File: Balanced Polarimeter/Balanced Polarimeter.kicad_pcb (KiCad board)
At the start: 2 copper layers, 65 x 46.5 mm, 23 parts, among them IC1 OP27, J1 73100-0105, J2 Conn_01x03_Pin, J3 Conn_01x02_Pin, J5 Conn_01x02_Pin, Q1 MMPQ3904, Q2 MMPQ3904, U1 ADA4898-1YRDZ, U2 ADA4898-1YRDZ

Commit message: Revised Wiring
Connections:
- D1 pad 1: Net-(D1-K) -> -5V
- D1 pad 3: +5V -> Net-(D1-A)
- D2 pad 1: Net-(D2-K) -> -5V
- D2 pad 3: +5V -> Net-(D2-A)
- Q1 pad 1: Net-(Q1-BASE_#2) -> Net-(D2-A)
- Q1 pad 13: Net-(Q1-BASE_#2) -> Net-(D2-A)
- Q1 pad 2: Net-(Q1-BASE_#2) -> Net-(D2-A)
- Q1 pad 3: Net-(D2-K) -> +5V
- Q1 pad 4: Net-(D2-K) -> +5V
- Q2 pad 1: Net-(Q2-BASE_#2) -> Net-(D1-A)
- Q2 pad 13: Net-(Q2-BASE_#2) -> Net-(D1-A)
- Q2 pad 2: Net-(Q2-BASE_#2) -> Net-(D1-A)
- Q2 pad 3: Net-(D1-K) -> +5V
- Q2 pad 4: Net-(D1-K) -> +5V
- R3 pad 2: Net-(U1--) -> Net-(Q1-COLLECTOR_#3_1)
- R4 pad 2: Net-(U2--) -> Net-(Q2-COLLECTOR_#3_1)
- U1 pad 2: Net-(U1--) -> Net-(Q1-COLLECTOR_#3_1)
- U1 pad 3: Net-(Q1-COLLECTOR_#3_1) -> GND
- U2 pad 2: Net-(U2--) -> Net-(Q2-COLLECTOR_#3_1)
- U2 pad 3: Net-(Q2-COLLECTOR_#3_1) -> GND
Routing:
- net -5V: track 105.2 -> 176.9 mm, vias 0 -> 1
- net Net-(Q1-COLLECTOR_#3_1): track 28.3 -> 59.9 mm, vias 2 -> 1
- net Net-(D1-A): track 0.00 -> 29.1 mm
- net Net-(D2-A): track 0.00 -> 27.1 mm
- net Net-(U1--): track 18.3 -> 0.00 mm
- net +5V: track 134.6 -> 119.4 mm
- net Net-(Q2-BASE_#1): track 3.42 -> 16.3 mm, vias 0 -> 2
- net Net-(D2-K): track 11.0 -> 0.00 mm
- net Net-(D1-K): track 10.5 -> 0.00 mm
- net Net-(R4-Pad1): track 15.7 -> 25.9 mm, vias 1 -> 0
- net Net-(Q1-BASE_#2): track 8.85 -> 0.00 mm
- net Net-(Q2-BASE_#2): track 8.85 -> 0.00 mm
- net Net-(U2--): track 8.04 -> 0.00 mm
- net Net-(Q1-BASE_#1): track 15.0 -> 20.6 mm, vias 0 -> 2
- net Net-(Q2-COLLECTOR_#3_1): track 26.0 -> 25.3 mm, vias 0 -> 1

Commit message: BNC Grounding
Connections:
- J1 pad 1: unconnected-(J1-Pad1) -> GND
- J1 pad 2: unconnected-(J1-Pad2) -> GND

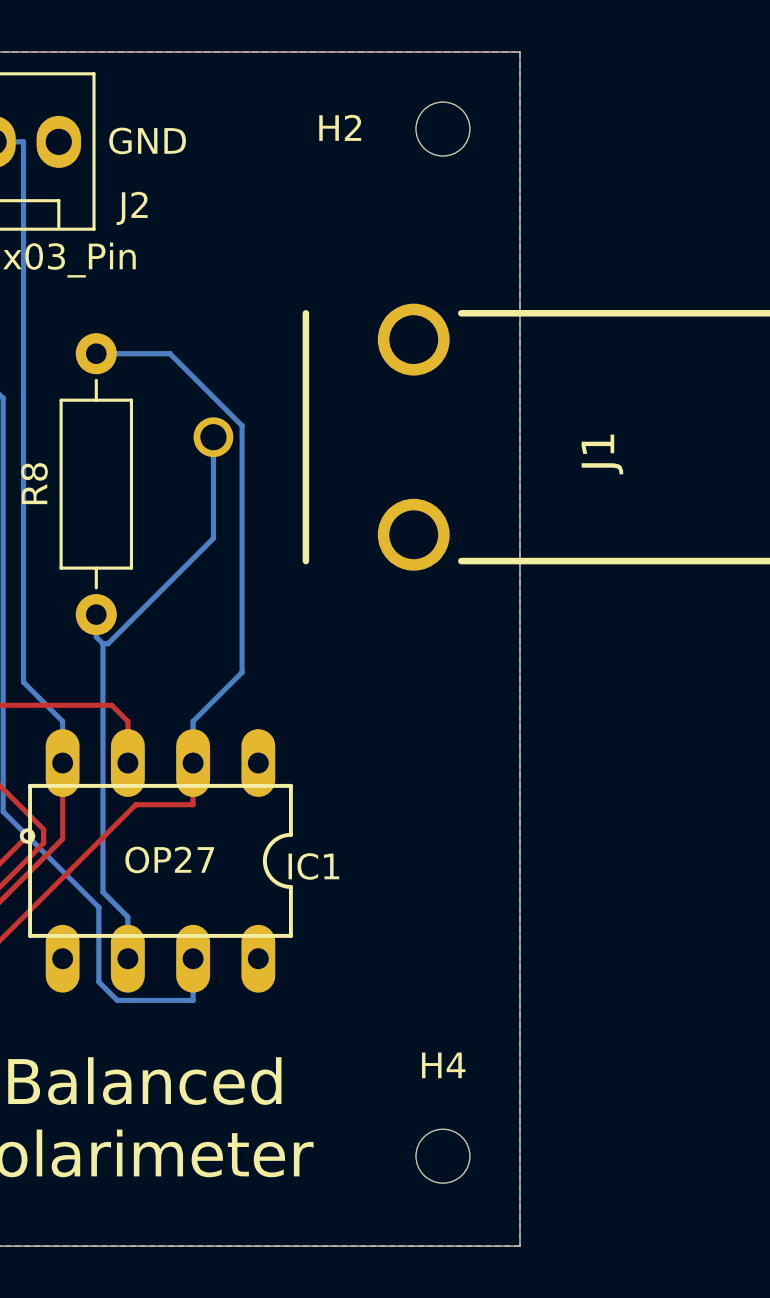
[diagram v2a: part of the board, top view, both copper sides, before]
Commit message: Changed H2 and H4 location
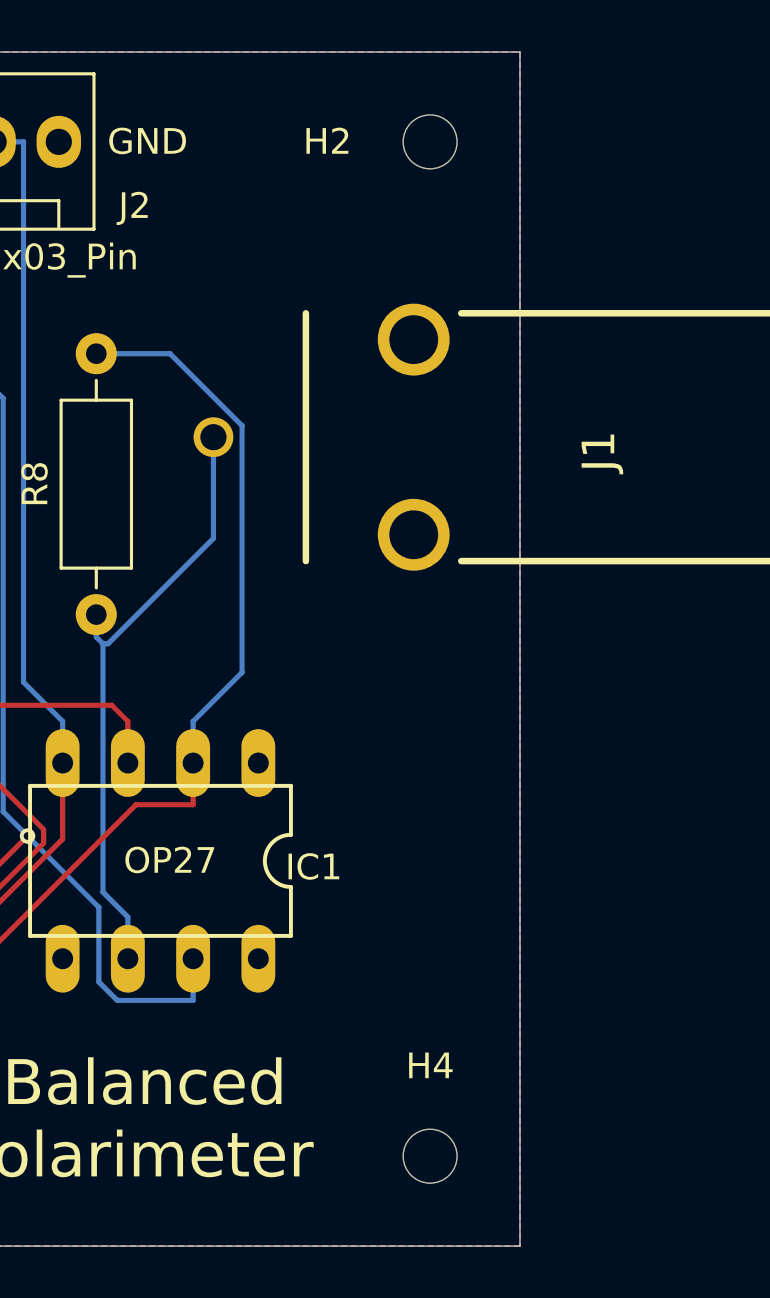
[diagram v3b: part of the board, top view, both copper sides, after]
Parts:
- moved H2 0.71 mm to (183.5, 65.0)
- moved H4 0.50 mm to (183.5, 104.5)
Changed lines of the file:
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@@
 	(footprint "MountingHole:MountingHole_2.1mm"
 		(layer "F.Cu")
-		(at 184 104.5)
+		(at 183.5 104.5)
 		(descr "Mounting Hole 2.1mm, no annular")
 		(tags "mounting hole 2.1mm no annular")
@@
 	(footprint "MountingHole:MountingHole_2.1mm"
 		(layer "F.Cu")
-		(at 184 64.5)
+		(at 183.5 65)
 		(descr "Mounting Hole 2.1mm, no annular")
 		(tags "mounting hole 2.1mm no annular")
